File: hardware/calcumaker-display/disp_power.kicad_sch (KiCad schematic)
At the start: 9 parts, among them U5 TPS61022RWUR, U6 74HCT125

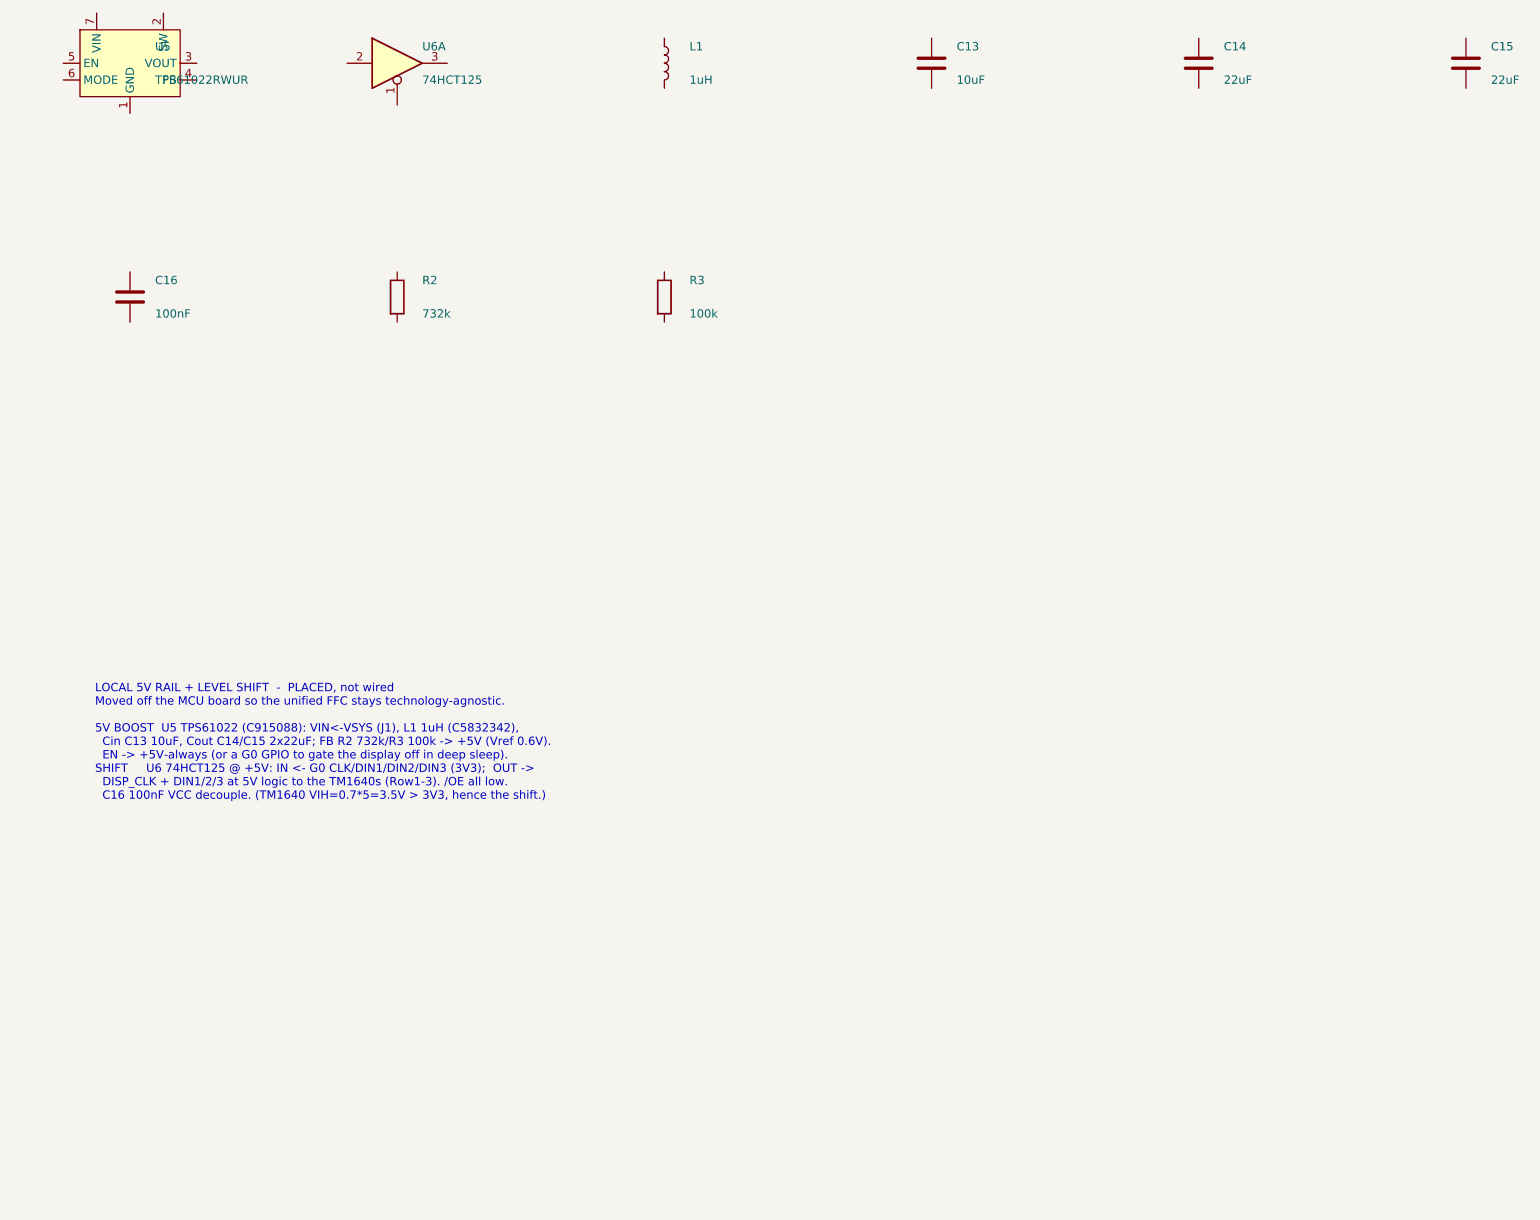
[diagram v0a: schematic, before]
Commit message: firmware: scaffold the two display-module targets + wire the module sheets
Firmware scaffold (all build; targets thumbv6m-none-eabi):
- calcumaker-display-proto: shared no_std wire protocol — the "display intent"
  DisplayFrame the U575 sends over SPI (text rows + flags + aux), with a
  fixed-length checksummed codec. Host-tested (cargo test: 3/3).
- calcumaker-display-fw: 7-seg module (STM32G031, embassy-stm32) — SPI-slave
  receiver + a bit-bang TM1640 driver + 7-seg render.
- calcumaker-matrix-fw: RGB-matrix module (RP2040, embassy-rp) — SPI-slave
  receiver + a 96x24 framebuffer/font blitter; WS2812 PIO output + SPI DMA
  stubbed as the bring-up TODOs.

Wire the one-off module schematic sheets (were placed-not-wired):
- kschgen: pin_geom now follows (extends ...) like pin_numbers, so derived
  symbols (STM32G031, 74xx) wire via net_pin.
- matrix rp2040 + rgb_power: RP2040 power/clock/flash/USB + the FET load switch
  and 3x single-gate level shifters are fully wired.
- display disp_mcu + disp_power: STM32G031 + the TPS61022 boost and 4x single-
  gate shifters are fully wired. (Quad 74xx buffers were multi-unit, which
  kschgen can't place fully, so the shifters are single-gate 74x1G125 — matching
  the keyboard's approach.)

All 4 boards check clean (mcu 46 / keyboard 179 / display 83 / matrix 2343, no
dup refs); wiring cut ERC pin_not_connected ~4x on both display modules.

Co-Authored-By: Claude Opus 4.8 (1M context) <noreply@anthropic.com>
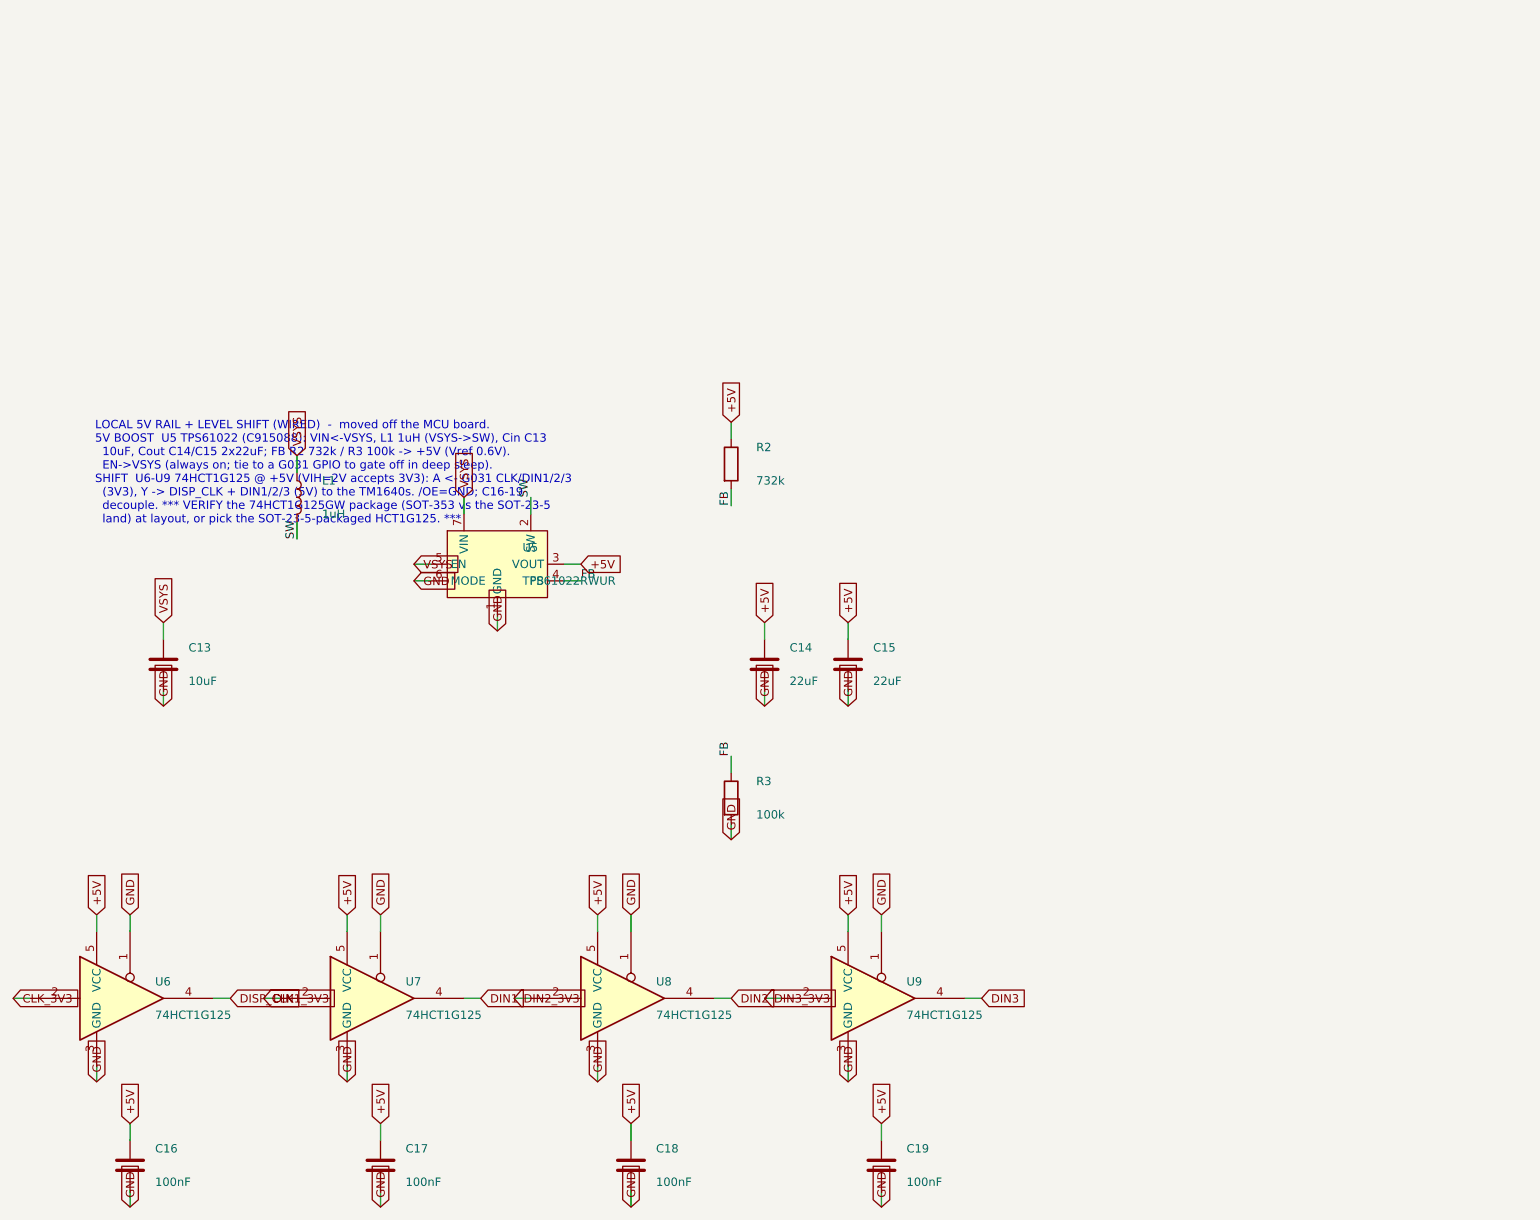
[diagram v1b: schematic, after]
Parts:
- removed U6: 74HCT125, Package_SO:SOIC-14_3.9x8.7mm_P1.27mm, symbol 74xx:74AHCT125
- added C17, C18, C19: 100nF, Capacitor_SMD:C_0402_1005Metric, symbol Device:C
- added U6, U7, U8, U9: 74HCT1G125, Package_TO_SOT_SMD:SOT-23-5, symbol 74xGxx:74LVC1G125
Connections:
- net GND: now reaches U5.1 (GND)
- net GND: now also C13.2, C14.2, C15.2, C16.2, R3.2, U5.6 (MODE), C17.2, C18.2, C19.2, U6.1, U6.3 (GND), U7.1, U7.3 (GND), U8.1, U8.3 (GND), U9.1, U9.3 (GND)
- net SW: now reaches U5.2 (SW)
- net SW: now also L1.2
- net +5V: now reaches U5.3 (VOUT)
- net +5V: now also C14.1, C15.1, C16.1, R2.1, C17.1, C18.1, C19.1, U6.5 (VCC), U7.5 (VCC), U8.5 (VCC), U9.5 (VCC)
- net FB: now reaches U5.4 (FB)
- net FB: now also R2.2, R3.1
- net VSYS: now reaches U5.5 (EN)
- net VSYS: now also C13.1, L1.1, U5.7 (VIN)
- new net CLK_3V3: U6.2
- new net DIN1: U7.4
- new net DIN1_3V3: U7.2
- new net DIN2: U8.4
- new net DIN2_3V3: U8.2
- new net DIN3: U9.4
- new net DIN3_3V3: U9.2
- new net DISP_CLK: U6.4
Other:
- note added: "LOCAL 5V RAIL + LEVEL SHIFT (WIRED) - moved off the MCU board. 5V BOOST U5 TPS61022 (C915088): VIN<-VSYS, L1 1uH (VSYS->SW), Cin C13 10uF, Cout C14/C15 2x22uF; FB R2 732k / R3 100k -> +5V (Vref 0.6V). EN->VSYS (always on; tie to a G031 GPIO to gate off in deep sleep). SHIFT U6-U9 74HCT1G125 @ +5V (VIH=2V accepts 3V3): A <- G031 CLK/DIN1/2/3 (3V3), Y -> DISP_CLK + DIN1/2/3 (5V) to the TM1640s. /OE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"
- note removed: "LOCAL 5V RAIL + LEVEL SHIFT - PLACED, not wired Moved off the MCU board so the unified FFC stays technology-agnostic. 5V BOOST U5 TPS61022 (C915088): VIN<-VSYS (J1), L1 1uH (C5832342), Cin C13 10uF, Cout C14/C15 2x22uF; FB R2 732k/R3 100k -> +5V (Vref 0.6V). EN -> +5V-always (or a G0 GPIO to gate the display off in deep sleep). SHIFT U6 74HCT125 @ +5V: IN <- G0 CLK/DIN1/DIN2/DIN3 (3V3); OUT -> DI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"
- title: Calcumaker 16 — Display — Local 5V boost (TPS61022) + 74HCT125 level shifter -> Calcumaker 16 — Display — Local 5V boost (TPS61022) + 4x 74HCT1G125 level shifter — wired
